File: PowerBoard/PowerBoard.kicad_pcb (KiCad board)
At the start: 2 copper layers, 20 x 20.5 mm, 7 parts, among them J1 PowerOut, P1 USB_C_Receptacle_USB2.0_14P, U1 MCP73811T-420I-OT

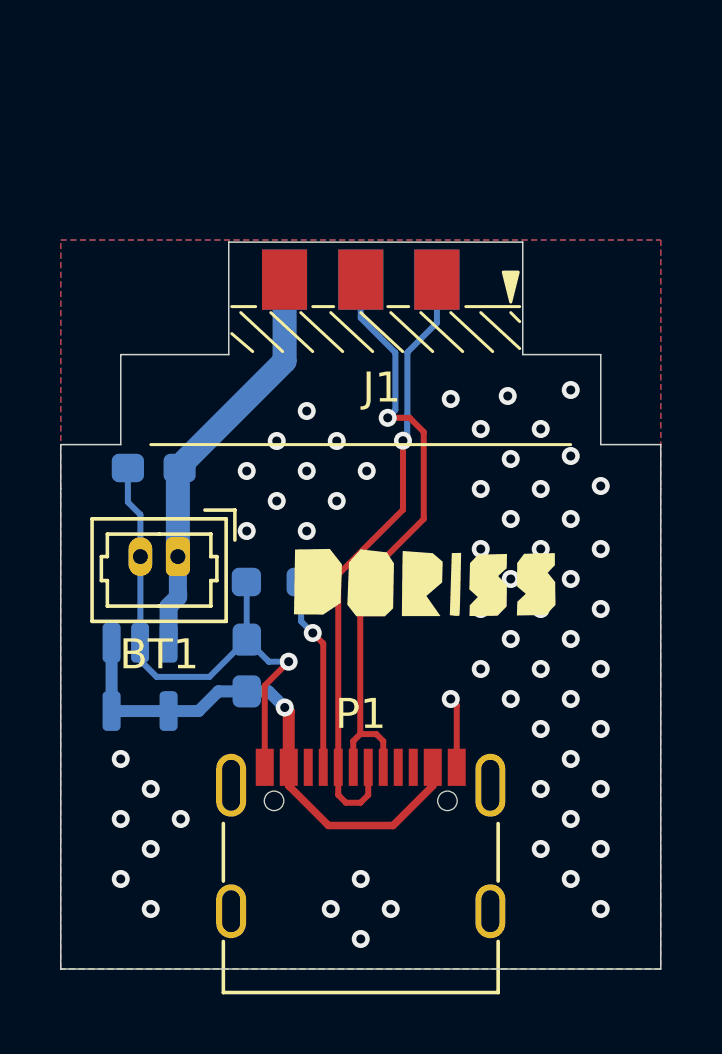
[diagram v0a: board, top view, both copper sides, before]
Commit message: Change location of tuch sensor, touch button now power up all components, change length. Add buzzer to mainboard and remove touch from them. change revision version
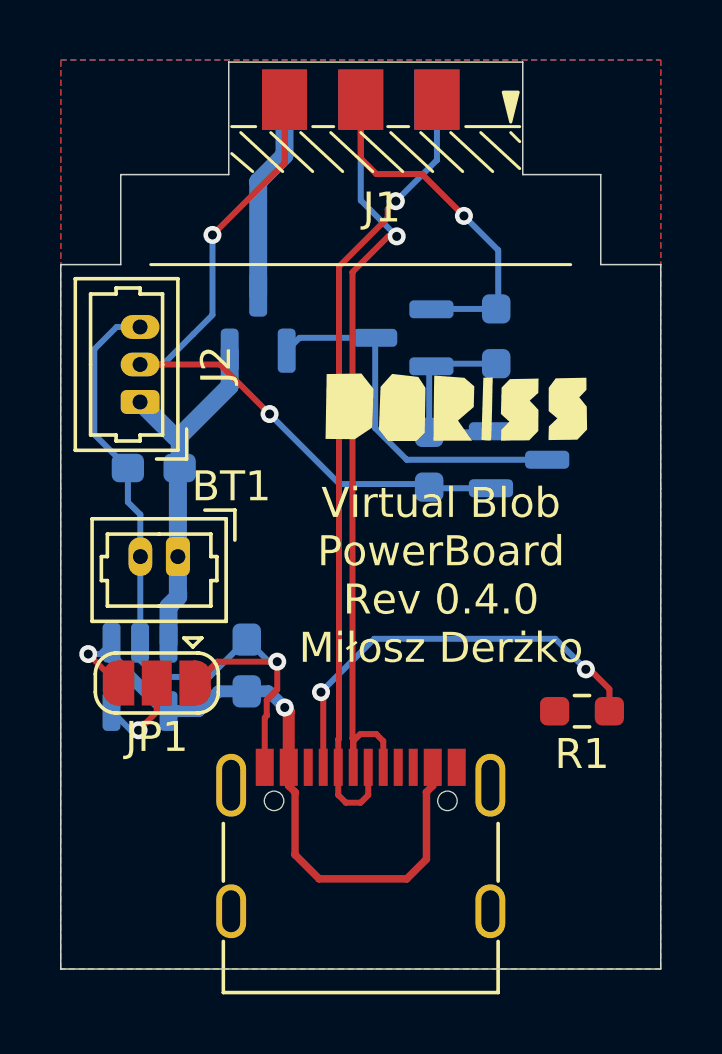
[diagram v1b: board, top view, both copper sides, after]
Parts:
- added J2: Touch, Connector_Molex:Molex_PicoBlade_53047-0310_1x03_P1.25mm_Vertical, F.Cu at (72.6, 71.1)
- added JP1: PROG_PIN, Jumper:SolderJumper-3_P1.3mm_Open_RoundedPad1.0x1.5mm, F.Cu at (73.2, 80.5)
- added Q1: AO3401A, Package_TO_SOT_SMD:SOT-23, B.Cu at (76.6, 68.5)
- added Q2: AO3400A, Package_TO_SOT_SMD:SOT-23, B.Cu at (85.3, 73.0)
- added Q3: AO3400A, Package_TO_SOT_SMD:SOT-23, B.Cu at (81.4, 69.0)
- added R2: 100k, Resistor_SMD:R_0603_1608Metric_Pad0.98x0.95mm_HandSolder, B.Cu at (82.3, 73.0)
- added R3: 100k, Resistor_SMD:R_0603_1608Metric_Pad0.98x0.95mm_HandSolder, B.Cu at (84.5, 68.9)
- R1: moved to F.Cu
- moved R1 11.1 mm to (87.4, 81.4)
- moved J1 6.00 mm to (80.0, 63.5)
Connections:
- J1 pad 1: +BATT -> /PWR_CONTROLLED
- J1 pad 4: unconnected-(J1-Pin_4-Pad4) -> /TOUCH
- J1 pad 5: unconnected-(J1-Pin_5-Pad5) -> /PWR_LATCH
- U1 pad 5: +5V -> Net-(JP1-C)
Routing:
- net /TOUCH: track 0.00 -> 24.7 mm, vias 0 -> 2
- net Net-(Q1-G): track 0.00 -> 12.3 mm
- net /PWR_LATCH: track 0.00 -> 12.0 mm, vias 0 -> 1
- net GND: track 20.7 -> 31.7 mm, vias 60 -> 1
- net Net-(P1-CC1): track 6.48 -> 14.3 mm, vias 1 -> 2
- net /PWR_CONTROLLED: track 0.00 -> 6.86 mm
- net /USB+: track 20.5 -> 26.5 mm
- net /USB-: track 20.7 -> 26.7 mm
- net +5V: track 17.7 -> 23.0 mm, vias 1 -> 2
- net Net-(JP1-C): track 0.00 -> 2.99 mm, vias 0 -> 1
- net +BATT: track 13.7 -> 12.4 mm
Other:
- board size 20 x 20.5 mm -> 20 x 26.5 mm
- board text added: "Virtual Blob PowerBoard Rev 0.4.0 Miłosz Derżko"
- board text removed: "Virtual Blob PowerBoard Rev 0.3.0 Miłosz Derżko"

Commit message: add buzer, update layout to schematic, make pcb mounting
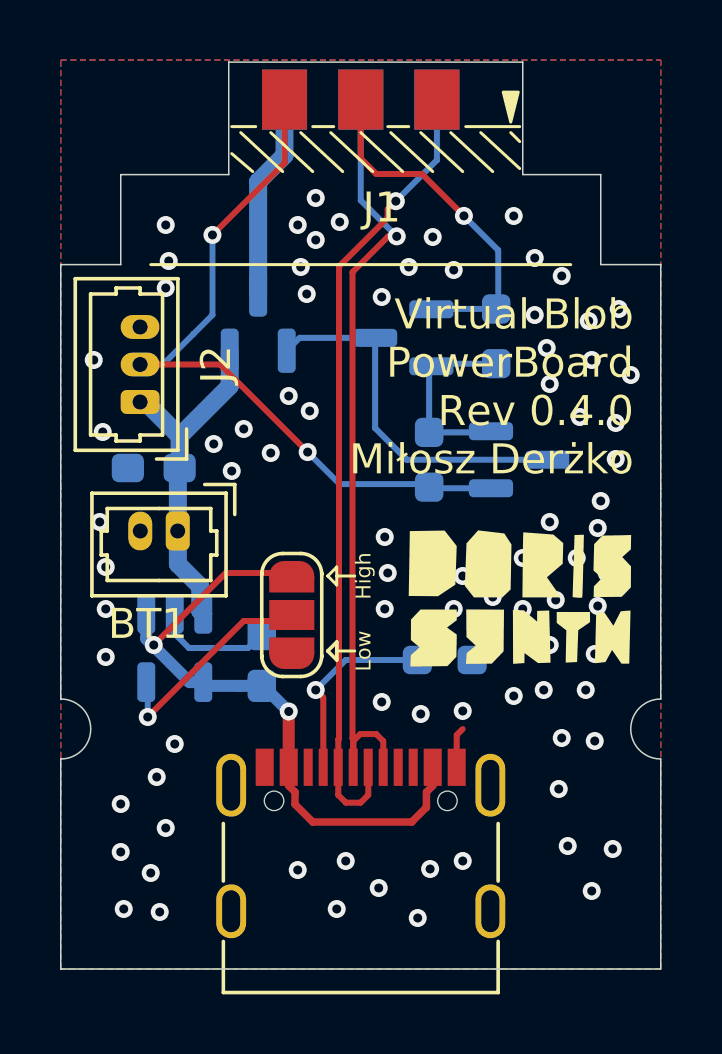
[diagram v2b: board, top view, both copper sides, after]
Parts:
- R1: moved to B.Cu
- moved JP1 5.04 mm to (77.7, 78.2), turned to 90 degrees
- moved R1 4.88 mm to (82.8, 79.7), turned to 0 degrees
- moved U1 1.51 mm to (73.8, 79.3)
- moved BT1 0.85 mm to (73.9, 75.4)
- moved C2 0.53 mm to (76.7, 79.7)
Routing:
- net GND: track 31.7 -> 11.8 mm, vias 1 -> 85
- net Net-(P1-CC1): track 14.3 -> 6.48 mm, vias 2 -> 1
- net Net-(JP1-C): track 2.99 -> 7.39 mm
- net +5V: track 23.0 -> 21.6 mm
- net +BATT: track 12.4 -> 11.6 mm
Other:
- outline, holes or cut-outs redrawn
- board text added: "High"
- board text added: "Low"
